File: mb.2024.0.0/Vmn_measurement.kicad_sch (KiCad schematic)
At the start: 28 parts, among them U2 OP07, U4 1115-Adress=0X49, U6 OP07, U7 OP07

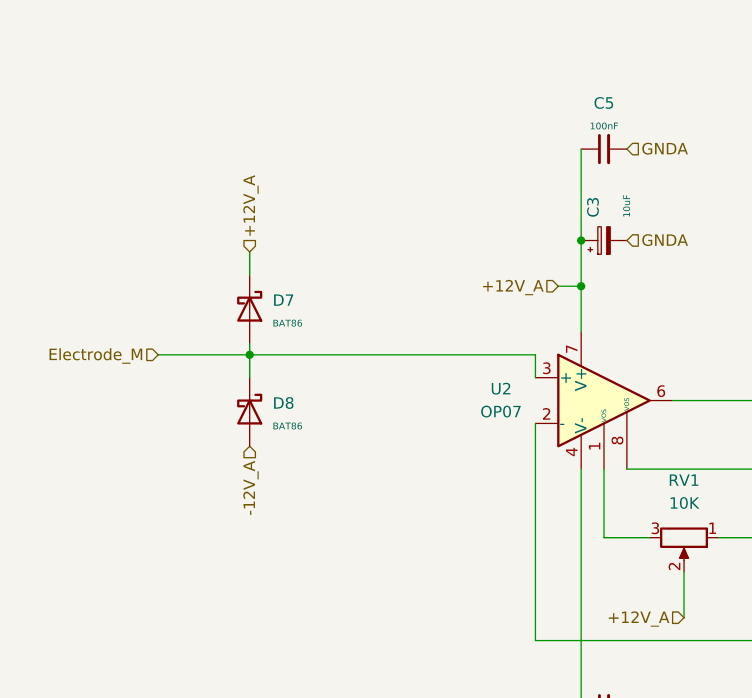
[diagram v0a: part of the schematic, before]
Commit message: update measurement board schematics and circuit
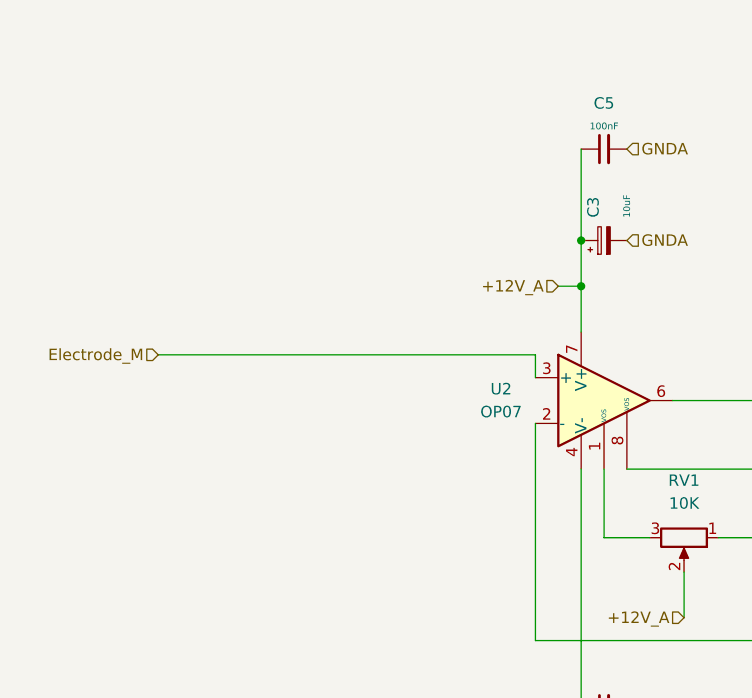
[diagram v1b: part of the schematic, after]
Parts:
- removed D7, D8: BAT86, Diode_THT:D_DO-35_SOD27_P7.62mm_Horizontal, symbol Diode:BAT86
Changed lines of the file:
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@@
   (junction (at 190.5 110.49) (diameter 0) (color 0 0 0 0)
-  )
-  (junction (at 88.9 175.26) (diameter 0) (color 0 0 0 0)
   )
   (junction (at 165.1 180.34) (diameter 0) (color 0 0 0 0)
@@
     (stroke (width 0) (type default) (color 0 0 0 0))
   )
-  (wire (pts (xy 88.9 163.83) (xy 88.9 166.37))
-    (stroke (width 0) (type default) (color 0 0 0 0))
-  )
   (wire (pts (xy 120.65 207.01) (xy 148.59 207.01))
     (stroke (width 0) (type default) (color 0 0 0 0))
@@
     (stroke (width 0) (type default) (color 0 0 0 0))
   )
-  (wire (pts (xy 88.9 175.26) (xy 88.9 177.8))
-    (stroke (width 0) (type default) (color 0 0 0 0))
-  )
   (wire (pts (xy 207.01 130.81) (xy 210.82 130.81))
     (stroke (width 0) (type default) (color 0 0 0 0))
@@
     (stroke (width 0) (type default) (color 0 0 0 0))
   )
-  (wire (pts (xy 88.9 175.26) (xy 120.65 175.26))
-    (stroke (width 0) (type default) (color 0 0 0 0))
-  )
   (wire (pts (xy 200.66 143.51) (xy 195.58 143.51))
     (stroke (width 0) (type default) (color 0 0 0 0))
@@
     (stroke (width 0) (type default) (color 0 0 0 0))
   )
-  (wire (pts (xy 88.9 173.99) (xy 88.9 175.26))
-    (stroke (width 0) (type default) (color 0 0 0 0))
-  )
   (wire (pts (xy 148.59 180.34) (xy 165.1 180.34))
     (stroke (width 0) (type default) (color 0 0 0 0))
@@
     (stroke (width 0) (type default) (color 0 0 0 0))
   )
-  (wire (pts (xy 78.74 175.26) (xy 88.9 175.26))
+  (wire (pts (xy 78.74 175.26) (xy 120.65 175.26))
     (stroke (width 0) (type default) (color 0 0 0 0))
   )
@@
     (effects (font (size 1.27 1.27)) (justify left))
   )
-  (hierarchical_label "+12V_A" (shape input) (at 88.9 163.83 90)
-    (effects (font (size 1.27 1.27)) (justify left))
-  )
   (hierarchical_label "5VA" (shape input) (at 210.82 217.17 90)
     (effects (font (size 1.27 1.27)) (justify left))
@@
   (hierarchical_label "+12V_A" (shape input) (at 137.16 204.47 180)
     (effects (font (size 1.27 1.27)) (justify right))
-  )
-  (hierarchical_label "-12V_A" (shape input) (at 88.9 185.42 270)
-    (effects (font (size 1.27 1.27)) (justify right))
-  )
-  (symbol (lib_id "Diode:BAT86") (at 88.9 181.61 270) (unit 1)
-    (in_bom yes) (on_board yes) (fields_autoplaced)
-    (property "Reference" "D8" (id 0) (at 91.44 180.6574 90)
-      (effects (font (size 1.27 1.27)) (justify left))
-    )
-    (property "Value" "BAT86" (id 1) (at 91.44 183.1974 90)
-      (effects (font (size 0.75 0.75)) (justify left))
-    )
-    (property "Footprint" "Diode_THT:D_DO-35_SOD27_P7.62mm_Horizontal" (id 2) (at 84.455 181.61 0)
-      (effects (font (size 1.27 1.27)) hide)
-    )
-    (property "Datasheet" "https://assets.nexperia.com/documents/data-sheet/BAT86.pdf" (id 3) (at 88.9 181.61 0)
-      (effects (font (size 1.27 1.27)) hide)
-    )
-    (pin "1")
-    (pin "2")
   )
   (symbol (lib_id "Device:C_Polarized_Small") (at 179.07 173.99 270) (unit 1)
@@
       (effects (font (size 1.27 1.27)) hide)
     )
-    (pin "1")
-    (pin "2")
-  )
-  (symbol (lib_id "Diode:BAT86") (at 88.9 170.18 270) (unit 1)
-    (in_bom yes) (on_board yes) (fields_autoplaced)
-    (property "Reference" "D7" (id 0) (at 91.44 169.2274 90)
-      (effects (font (size 1.27 1.27)) (justify left))
-    )
-    (property "Value" "BAT86" (id 1) (at 91.44 171.7674 90)
-      (effects (font (size 0.75 0.75)) (justify left))
-    )
-    (property "Footprint" "Diode_THT:D_DO-35_SOD27_P7.62mm_Horizontal" (id 2) (at 84.455 170.18 0)
-      (effects (font (size 1.27 1.27)) hide)
-    )
-    (property "Datasheet" "https://assets.nexperia.com/documents/data-sheet/BAT86.pdf" (id 3) (at 88.9 170.18 0)
-      (effects (font (size 1.27 1.27)) hide)
-    )
